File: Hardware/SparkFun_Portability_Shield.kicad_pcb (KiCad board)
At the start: 2 copper layers, 43.2 x 43.2 mm, 92 parts, among them J1 microSD_Friction, J2 1x10, J3 JST_2mm_LiPo, J4 1x09, SW2 Nav Switch, U1 AP2112K-3.3, U2 MAX17048, U3 MCP73831, U4 PCA9557PW, U5 OLED_1.3"

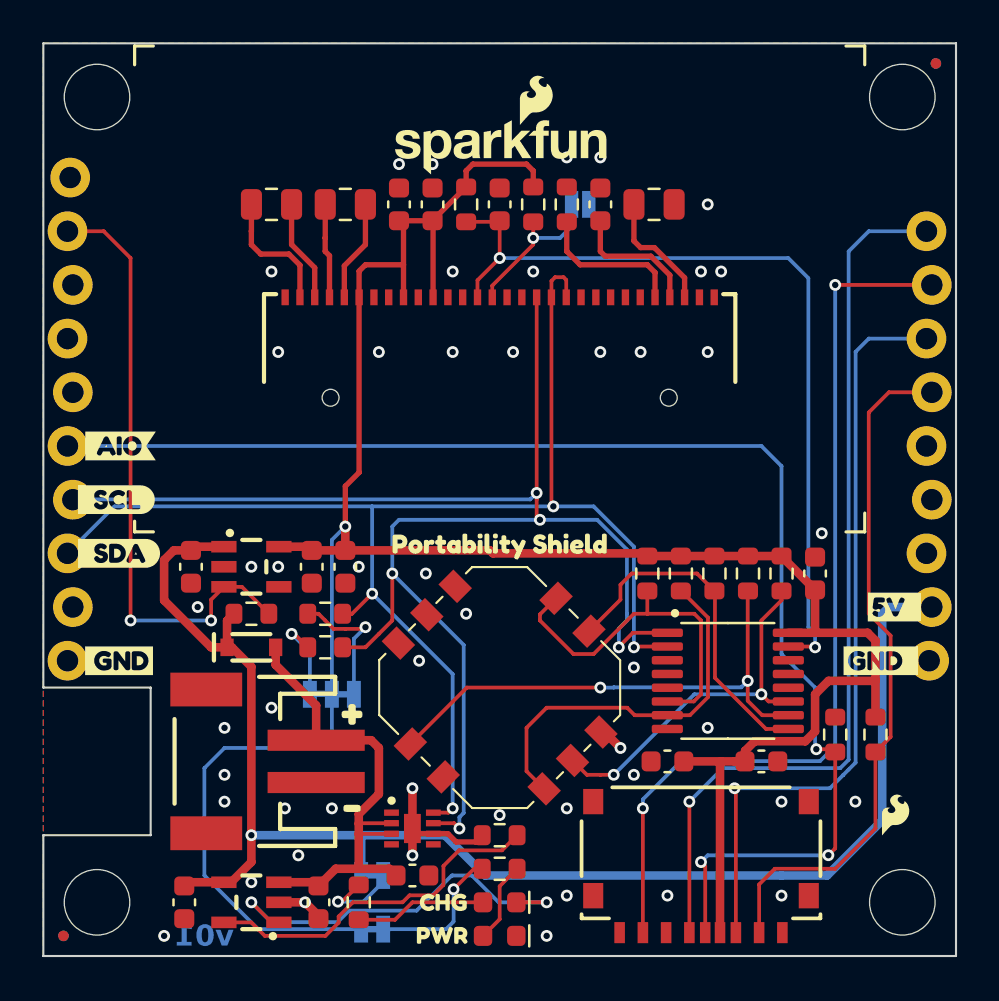
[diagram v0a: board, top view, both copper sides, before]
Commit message: Fix nav switch. Adjust silk. Update to v10.
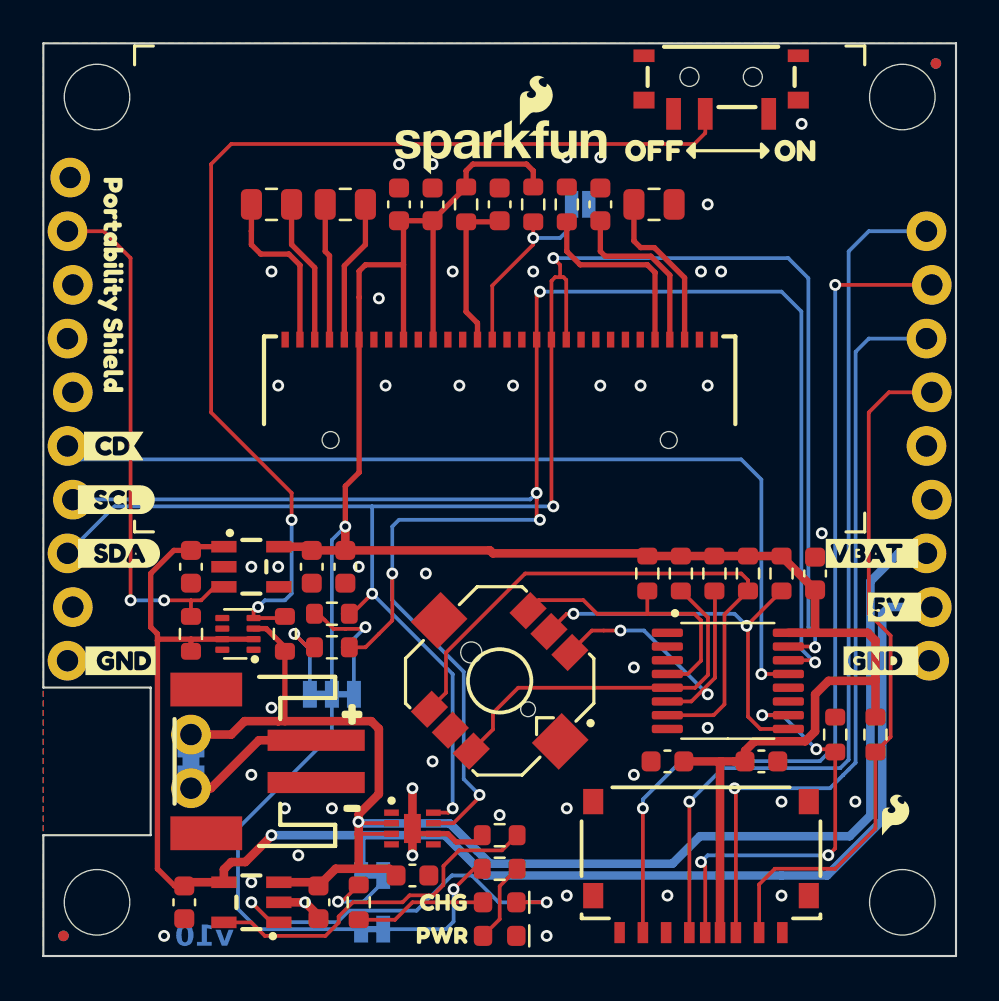
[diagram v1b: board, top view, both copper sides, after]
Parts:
- removed D2: BAT60A, SparkFun-Semiconductor-Standard:SOD-323
- removed kibuzzard-66CAA432 (x2): G***, kibuzzard-66CAA432
- removed kibuzzard-66F377AE: G***, kibuzzard-66F377AE
- removed kibuzzard-66F3797E: G***, kibuzzard-66F3797E
- added JP5: MEAS, SparkFun-Jumper:Jumper_2_PTH_SMD_Combo-NC, B.Cu at (142.2, 108.3)
- added R17: 100k, SparkFun-Resistor:R_0603_1608Metric, F.Cu at (146.7, 102.2)
- added SW1: SPDT_Slide_SMD_6.7x2.6mm, SparkFun-Switch:Slide_SPST_SMD_6.7x2.6mm, F.Cu at (167.3, 75.9)
- added U7: LM66200, SparkFun-Semiconductor-Standard:SOT-583-8, F.Cu at (144.5, 102.2)
- added kibuzzard-66F4A593: G***, kibuzzard-66F4A593, B.Cu at (138.6, 93.3)
- added kibuzzard-66F4A59B: G***, kibuzzard-66F4A59B, F.Cu at (138.6, 93.3)
- added kibuzzard-67140B1C: G***, kibuzzard-67140B1C, F.Cu at (170.8, 79.4)
- added kibuzzard-67140B1C: G***, kibuzzard-67140B1C, B.Cu at (170.8, 76.8)
- added kibuzzard-67140B31: G***, kibuzzard-67140B31, F.Cu at (164.1, 79.4)
- added kibuzzard-67140B31: G***, kibuzzard-67140B31, B.Cu at (164.1, 76.8)
- added kibuzzard-67140CF9: G***, kibuzzard-67140CF9, B.Cu at (167.3, 78.7)
- added kibuzzard-673B98BA: G***, kibuzzard-673B98BA, F.Cu at (174.5, 98.4)
- added kibuzzard-673B9939: G***, kibuzzard-673B9939, B.Cu at (174.5, 98.4)
- added kibuzzard-673B9961: G***, kibuzzard-673B9961, F.Cu at (138.9, 103.5)
- added kibuzzard-673B9979: G***, kibuzzard-673B9979, B.Cu at (138.9, 103.5)
- added kibuzzard-673B999B: G***, kibuzzard-673B999B, B.Cu at (144.1, 108.3)
- SW2: footprint SparkFun-Switch:Navigation_SMD_9.9x9.9mm -> SparkFun-Switch:Navigation_SMD_7.5x7.5mm
- U4: value PCA9557PW -> PCA9554PW
- moved kibuzzard-66F083A9 22.2 mm to (138.4, 85.7), turned to -90 degrees
- moved kibuzzard-66F08248 3.33 mm to (156.8, 94.8)
- moved G*** 3.18 mm to (157.0, 90.2)
- moved kibuzzard-66F0824D 3.17 mm to (156.8, 97.2)
- moved R13 3.01 mm to (142.2, 102.2), turned to 90 degrees
- moved SW2 0.32 mm to (156.8, 104.5)
- moved R15 0.32 mm to (148.9, 102.9)
- moved R16 0.32 mm to (148.9, 101.3)
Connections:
- C6 pad 1: ~{RESET}_P -> OLED_~{RESET}
- J2 pad 6: SD_CD -> GPIO_~{INT}
- J3 pad 2: VBATT -> Net-(J3-+)
- J4 pad 3: unconnected-(J4-Pin_7-Pad3) -> VBATT
- J4 pad 4: Main-RX -> unconnected-(J4-Pad4)
- J4 pad 5: Main-TX -> unconnected-(J4-Pad5)
- R1 pad 1: ~{RESET}_P -> OLED_~{RESET}
- SW2 pad 1: SW_Up -> SW_Left
- SW2 pad 2: SW_Right -> GND
- SW2 pad 3: GND -> SW_Down
- SW2 pad 4: SW_Center -> SW_Right
- SW2 pad 5: SW_Down -> SW_Center
- SW2 pad 6: GND -> SW_Up
- U4 pad 1: SCL -> GND
- U4 pad 10: SW_Left -> SD_CD
- U4 pad 11: SW_Center -> unconnected-(U4-IO6-Pad11)
- U4 pad 13: unconnected-(U4-IO6-Pad13) -> GPIO_~{INT}
- U4 pad 14: unconnected-(U4-IO7-Pad14) -> SCL
- U4 pad 15: ~{RESET}_P -> SDA
- U4 pad 2: SDA -> GND
- U4 pad 4: GND -> SW_Up
- U4 pad 5: GND -> SW_Down
- U4 pad 6: SW_Up -> SW_Right
- U4 pad 7: SW_Down -> SW_Left
- U4 pad 9: SW_Right -> SW_Center
- U5 pad 14: ~{RESET}_P -> OLED_~{RESET}
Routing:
- net Net-(U7-~{ON}): track 0.00 -> 50.8 mm, vias 0 -> 2
- net VBATT: track 23.6 -> 71.1 mm, vias 0 -> 1
- net GPIO_~{INT}: track 0.00 -> 44.0 mm, vias 0 -> 1
- net SD_CD: track 63.8 -> 20.1 mm, vias 3 -> 4
- net ~{RESET}_P: track 39.5 -> 0.00 mm, vias 2 -> 0
- net SDA: track 65.9 -> 89.3 mm, vias 4 -> 5
- net SCL: track 74.1 -> 93.4 mm, vias 5 -> 6
- net OLED_~{RESET}: track 0.00 -> 7.40 mm
- net Net-(J3-+): track 0.00 -> 6.86 mm
- net 5V: track 70.9 -> 75.6 mm
- net 3V3_EN: track 29.0 -> 25.1 mm
- net SW_Left: track 24.6 -> 28.2 mm, vias 2 -> 0
- net SW_Up: track 16.9 -> 13.6 mm
- net Net-(U5-VCOMH): track 6.25 -> 8.25 mm
- net Net-(U5-VCC): track 5.77 -> 7.77 mm
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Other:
- board text added: "v10"
- board text removed: "v01"

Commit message: Update I2C address on PCA9554
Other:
- board text added: "Finish: Lead-Free HASL"
- board text removed: "Finish: HASL"
- board text removed: "Material: TG155"
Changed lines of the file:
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@@
 		(sheetname "Root")
 		(sheetfile "SparkFun_Portability_Shield.kicad_sch")
-		(attr exclude_from_bom)
+		(attr exclude_from_pos_files exclude_from_bom)
 		(fp_text user " https://creativecommons.org/licenses/by-sa/4.0/"
 			(at 0 1.27 0)
@@
 		(fp_arc
 			(start 0.762 -1.016)
-			(mid 1.08529 -0.88209)
+			(mid 1.085289 -0.882089)
 			(end 1.2192 -0.5588)
 			(stroke
@@
 		(fp_arc
 			(start 0.762 -1.016)
-			(mid 1.08529 -0.88209)
+			(mid 1.085289 -0.882089)
 			(end 1.2192 -0.5588)
 			(stroke
@@
 		)
 	)
-	(gr_text "Material: TG155"
-		(at 224.4725 180.6575 0)
-		(layer "F.Fab")
-		(effects
-			(font
-				(size 1.27 1.27)
-				(thickness 0.15)
-			)
-			(justify left bottom)
-		)
-	)
 	(gr_text "Outer Copper Weight: 1oz"
 		(at 224.4725 184.4675 0)
@@
 		)
 	)
-	(gr_text "Finish: HASL"
+	(gr_text "Finish: Lead-Free HASL"
 		(at 193.9925 186.3725 0)
 		(layer "F.Fab")
